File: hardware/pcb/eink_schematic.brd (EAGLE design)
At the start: 160 x 100 mm, 2 parts, among them U1 NUCLEUM

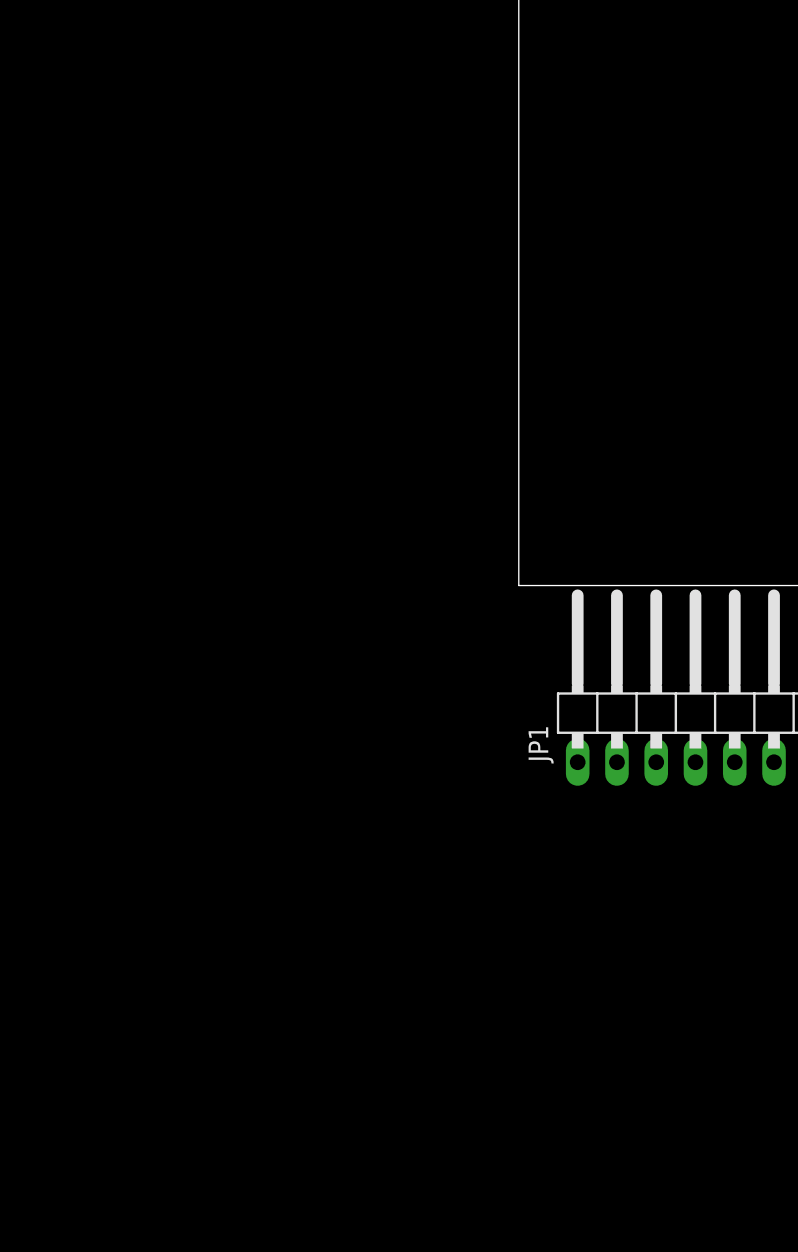
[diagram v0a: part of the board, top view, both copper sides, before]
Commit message: added buck/boost regulator to schematic
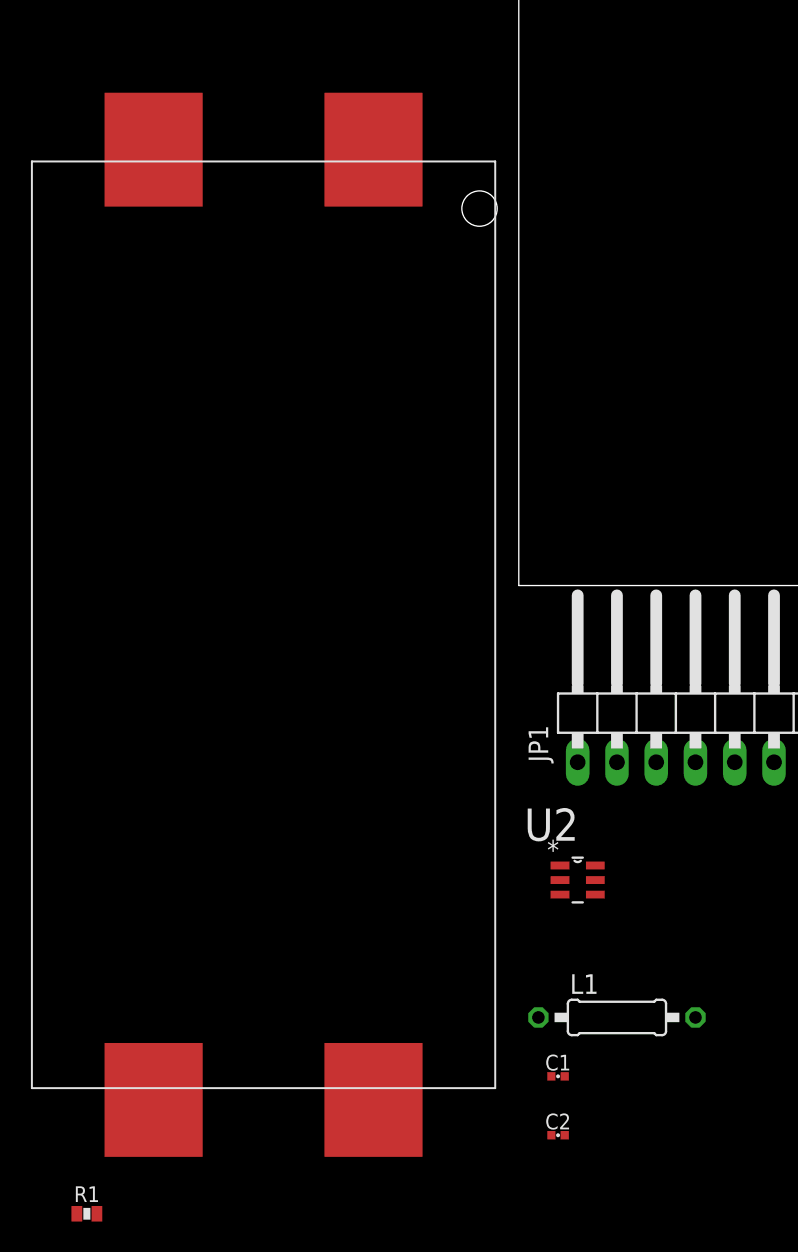
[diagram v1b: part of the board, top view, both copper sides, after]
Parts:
- added C1: 2.2uF, passives:0402_CAP
- added C2: 10uF, passives:0402_CAP
- added J1: AA_BAT_PACKSMD, connector:AA_SMD
- added L1: 10uH, umich:0207/10
- added R1: 100K, passives:0603-RES
- added U2: LTC3531ES6-3PBF, LTC_By_element14_Batch_1:SOT95P280X100-6N
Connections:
- new net N$1: L1.1, U2.6
- new net N$2: L1.2, U2.1
- new net N$4: C1.1, J1.2+, R1.2, U2.5
- new net N$5: J1.1+, J1.2-
- new net N$6: R1.1, U2.4
- net GND: now also C1.2, C2.2, J1.1-, U2.2
- net VCC: now also C2.1, U2.3
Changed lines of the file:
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@@
 <element name="U1" library="nucleum" package="NUCLEUM" value="NUCLEUM" x="0" y="44.45"/>
 <element name="JP1" library="pinhead" package="1X10/90" value="" x="15.24" y="-7.62"/>
+<element name="U2" library="LTC_By_element14_Batch_1" package="SOT95P280X100-6N" value="LTC3531ES6-3PBF" x="3.81" y="-19.05">
+<attribute name="PACKAGE" value="TSOT-23-6" x="3.81" y="-19.05" size="1.778" layer="27" display="off"/>
+<attribute name="OC_NEWARK" value="46P4583" x="3.81" y="-19.05" size="1.778" layer="27" display="off"/>
+<attribute name="MPN" value="LTC3531ES6-3#PBF" x="3.81" y="-19.05" size="1.778" layer="27" display="off"/>
+<attribute name="SUPPLIER" value="Linear Technology" x="3.81" y="-19.05" size="1.778" layer="27" display="off"/>
+<attribute name="OC_FARNELL" value="-" x="3.81" y="-19.05" size="1.778" layer="27" display="off"/>
+</element>
+<element name="L1" library="umich" package="0207/10" value="10uH" x="6.35" y="-27.94"/>
+<element name="C1" library="passives" package="0402_CAP" value="2.2uF" x="2.54" y="-31.75"/>
+<element name="C2" library="passives" package="0402_CAP" value="10uF" x="2.54" y="-35.56"/>
+<element name="J1" library="connector" package="AA_SMD" value="AA_BAT_PACKSMD" x="-16.51" y="-2.54"/>
+<element name="R1" library="passives" package="0603-RES" value="100K" x="-27.94" y="-40.64"/>
 </elements>
 <signals>
@@
 <contactref element="JP1" pad="1"/>
 <contactref element="JP1" pad="10"/>
+<contactref element="C2" pad="2"/>
+<contactref element="U2" pad="2"/>
+<contactref element="J1" pad="1-"/>
+<contactref element="C1" pad="2"/>
 <wire x1="3.81" y1="-11.43" x2="8.4811" y2="62.4989" width="0" layer="19" extent="1-1"/>
+<wire x1="2.667" y1="-19.05" x2="3.81" y2="-11.43" width="0" layer="19" extent="1-1"/>
+<wire x1="2.97306875" y1="-31.75" x2="2.667" y2="-19.05" width="0" layer="19" extent="1-1"/>
+<wire x1="2.97306875" y1="-35.56" x2="2.97306875" y2="-31.75" width="0" layer="19" extent="1-1"/>
 <wire x1="26.67" y1="-11.43" x2="3.81" y2="-11.43" width="0" layer="19" extent="1-1"/>
+<wire x1="-23.622" y1="-33.274" x2="2.97306875" y2="-31.75" width="0" layer="19" extent="1-1"/>
 </signal>
 <signal name="VCC">
@@
 <contactref element="JP1" pad="3"/>
 <contactref element="JP1" pad="4"/>
+<contactref element="U2" pad="3"/>
+<contactref element="C2" pad="1"/>
 <wire x1="8.89" y1="-11.43" x2="8.4811" y2="44.3411" width="0" layer="19" extent="1-1"/>
 <wire x1="11.43" y1="-11.43" x2="8.89" y2="-11.43" width="0" layer="19" extent="1-1"/>
+<wire x1="2.667" y1="-19.9898" x2="8.89" y2="-11.43" width="0" layer="19" extent="1-1"/>
+<wire x1="2.10693125" y1="-35.56" x2="2.667" y2="-19.9898" width="0" layer="19" extent="1-1"/>
+</signal>
+<signal name="N$1">
+<contactref element="L1" pad="1"/>
+<contactref element="U2" pad="6"/>
+<wire x1="4.953" y1="-18.1102" x2="1.27" y2="-27.94" width="0" layer="19" extent="1-1"/>
+</signal>
+<signal name="N$2">
+<contactref element="L1" pad="2"/>
+<contactref element="U2" pad="1"/>
+<wire x1="2.667" y1="-18.1102" x2="11.43" y2="-27.94" width="0" layer="19" extent="1-1"/>
+</signal>
+<signal name="N$5">
+<contactref element="J1" pad="1+"/>
+<contactref element="J1" pad="2-"/>
+<wire x1="-23.622" y1="28.194" x2="-9.398" y2="28.194" width="0" layer="19" extent="1-1"/>
+</signal>
+<signal name="N$4">
+<contactref element="J1" pad="2+"/>
+<contactref element="U2" pad="5"/>
+<contactref element="C1" pad="1"/>
+<contactref element="R1" pad="2"/>
+<wire x1="-9.398" y1="-33.274" x2="-27.29" y2="-40.64" width="0" layer="19" extent="1-1"/>
+<wire x1="2.10693125" y1="-31.75" x2="-9.398" y2="-33.274" width="0" layer="19" extent="1-1"/>
+<wire x1="4.953" y1="-19.05" x2="2.10693125" y2="-31.75" width="0" layer="19" extent="1-1"/>
+</signal>
+<signal name="N$6">
+<contactref element="U2" pad="4"/>
+<contactref element="R1" pad="1"/>
+<wire x1="4.953" y1="-19.9898" x2="-28.59" y2="-40.64" width="0" layer="19" extent="1-1"/>
 </signal>
 </signals>

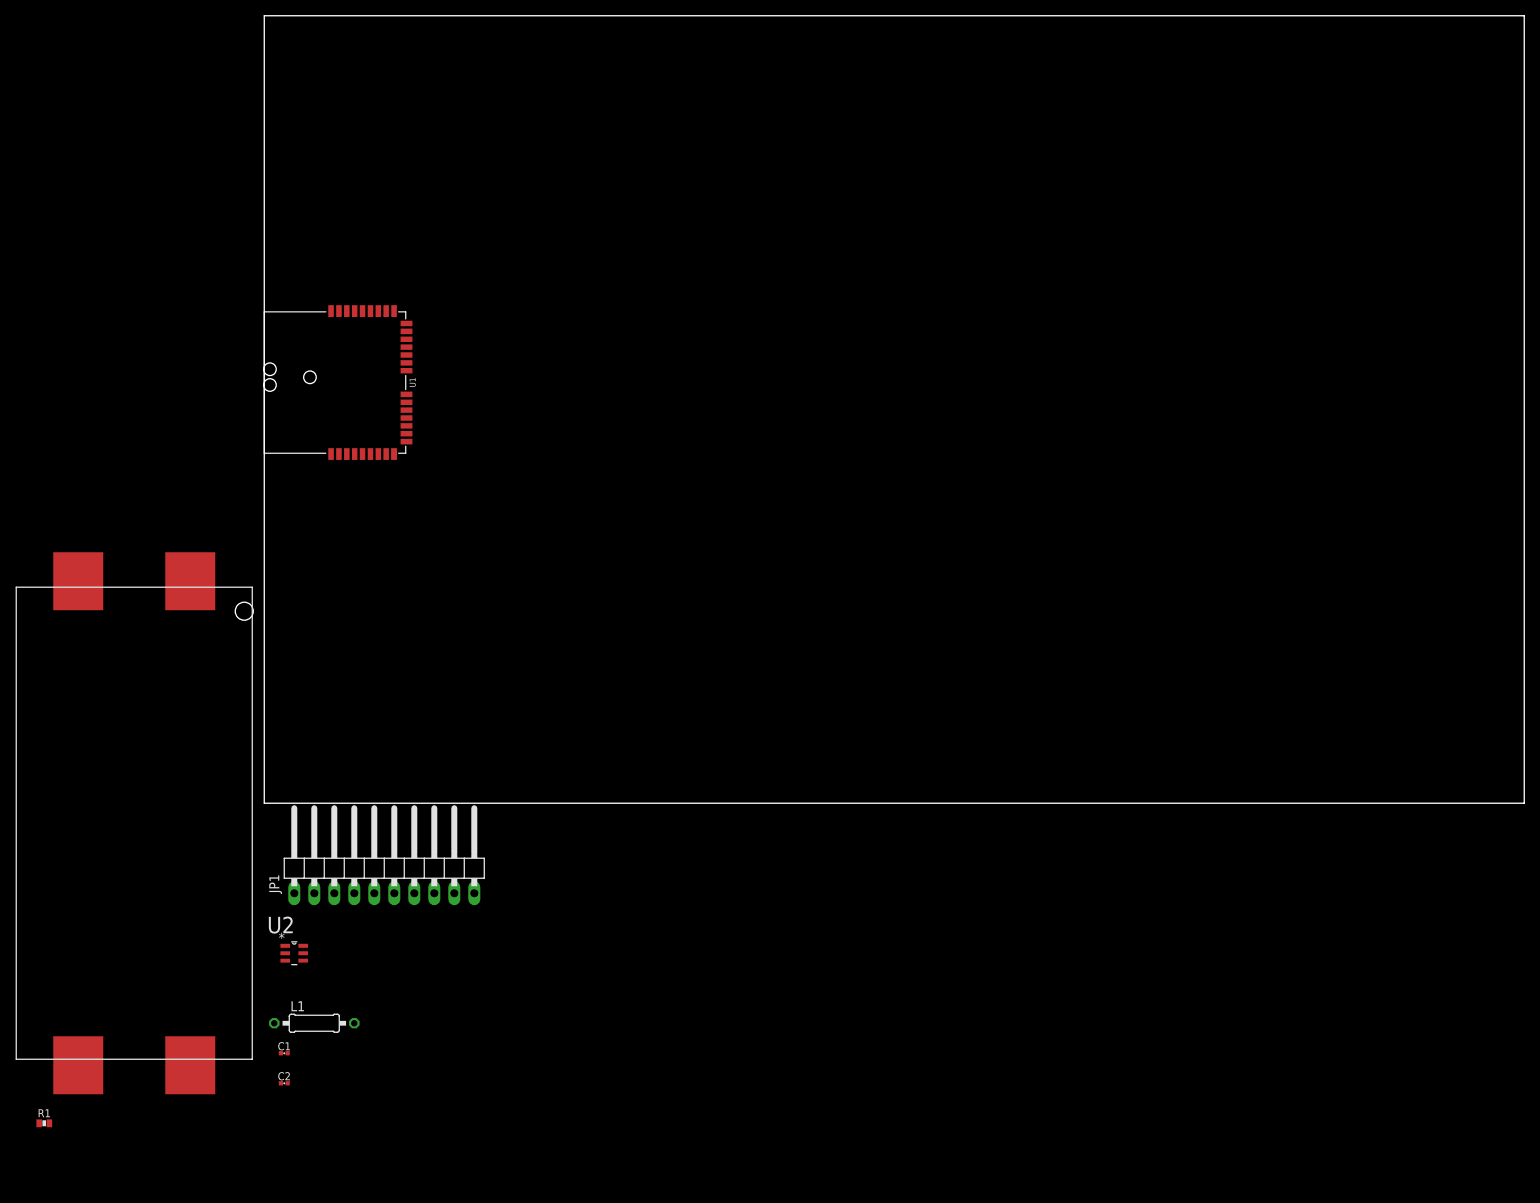
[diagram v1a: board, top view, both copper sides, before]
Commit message: Added some libs, buck/boost regulator, and barrel jack
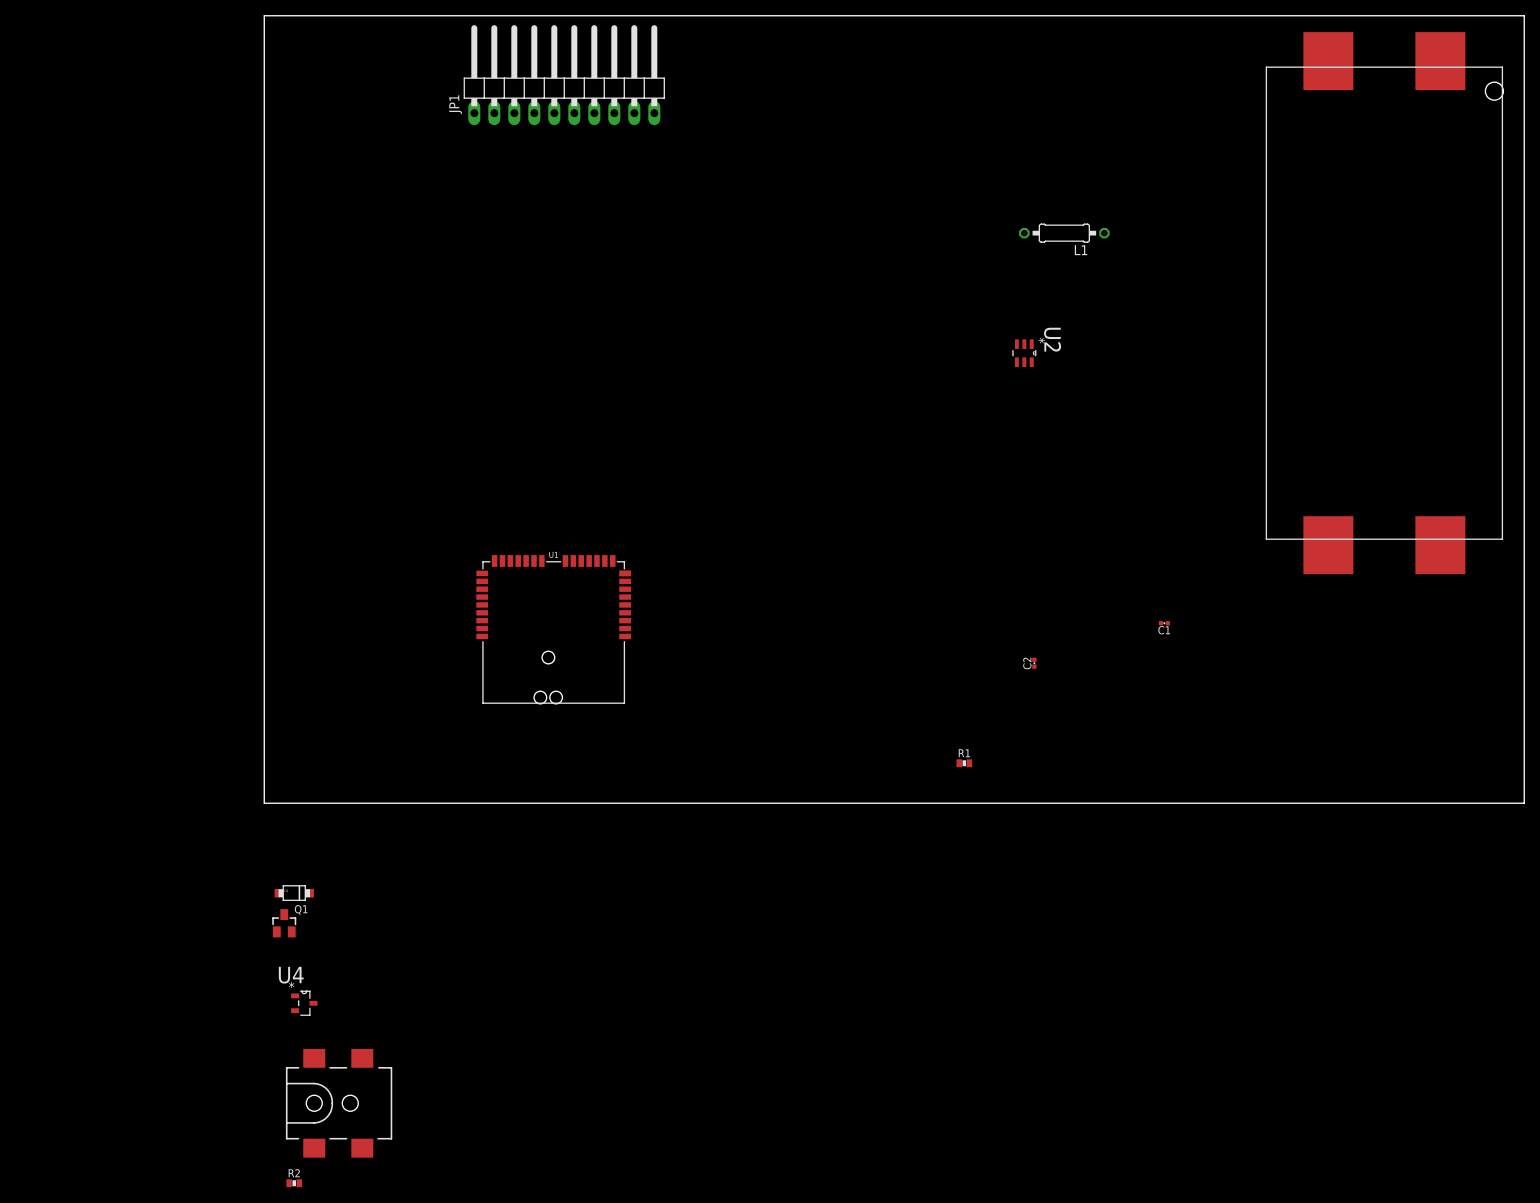
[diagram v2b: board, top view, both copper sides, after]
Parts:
- added D1: (no value), nxp:SOD123W
- added J2: 5.5x2.1mm Barrel, SparkFun-Connectors:POWER_JACK_SMD
- added Q1: FDN340P, transistor-fet:SSOT-3
- added R2: 100K, passives:0603-RES
- added U4: MAX6326UR29+, Maxim_By_element14_Batch_1:SOT95P228X119-3N
- moved J1 171.9 mm to (142.2, 63.5)
- moved L1 138.3 mm to (101.6, 72.4), turned to 180 degrees
- moved R1 125.5 mm to (88.9, 5.08)
- moved C1 124.4 mm to (114.3, 22.9), turned to 180 degrees
- moved U2 120.0 mm to (96.5, 57.1), turned to 270 degrees
- moved C2 109.2 mm to (97.8, 17.8), turned to 90 degrees
- moved JP1 101.7 mm to (38.1, 91.4)
- moved U1 55.7 mm to (45.7, 12.7), turned to 90 degrees
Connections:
- net N$1 renamed SW1
- net N$2 renamed SW2
- net N$6 renamed !SHDN
- new net N$1: Q1.1, U4.2
- new net N$2: D1.P$1, J2.VIN0, R2.1, U4.3
- new net N$3: C1.1, D1.P$2, Q1.2, R1.2, U2.5
- net GND: now also R2.2, U4.1
- net N$4: now also Q1.3; no longer C1.1, R1.2, U2.5

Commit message: Created L-shaped board
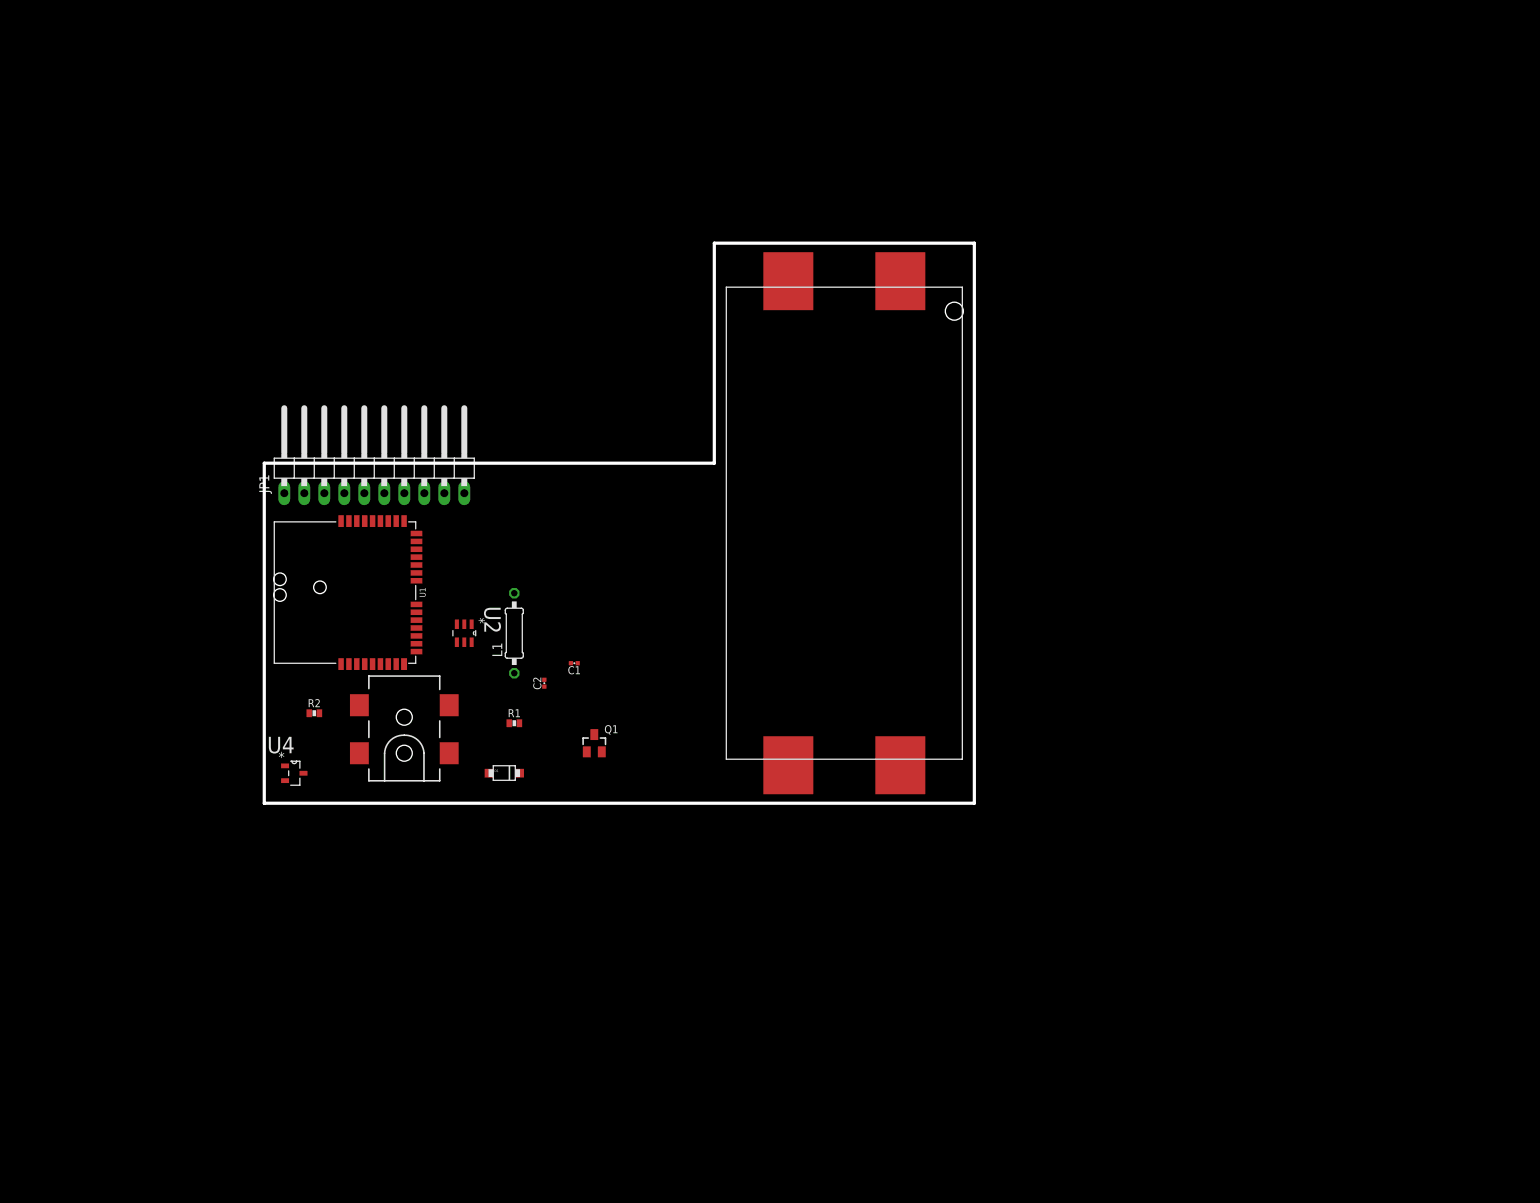
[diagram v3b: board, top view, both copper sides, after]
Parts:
- moved L1 86.4 mm to (31.8, 21.6), turned to 90 degrees
- moved U2 79.5 mm to (25.4, 21.6)
- moved C1 75.1 mm to (39.4, 17.8)
- moved J1 74.1 mm to (73.7, 35.6)
- moved C2 62.3 mm to (35.6, 15.2)
- moved R2 59.7 mm to (6.35, 11.4)
- moved R1 57.4 mm to (31.8, 10.2)
- moved JP1 54.0 mm to (14.0, 43.2)
- moved J2 45.9 mm to (17.8, 6.35), turned to 90 degrees
- moved Q1 45.5 mm to (41.9, 7.62)
- moved U1 44.7 mm to (1.27, 17.8), turned to 0 degrees
- moved D1 30.7 mm to (30.5, 3.81)
- moved U4 29.2 mm to (3.81, 3.81)
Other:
- board size 160 x 100 mm -> 90.2 x 71.1 mm
